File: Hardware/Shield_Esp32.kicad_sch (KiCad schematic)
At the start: 47 parts, among them J1 Conn_01x02_Male, J10 Conn_01x02_Male, J11 Conn_01x02_Male, J12 Conn_01x02_Male, J13 Conn_01x02_Male, J14 Conn_01x02_Male, J15 Conn_01x02_Male, J16 Conn_01x02_Male, J17 Conn_01x02_Male, J18 Conn_01x02_Male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

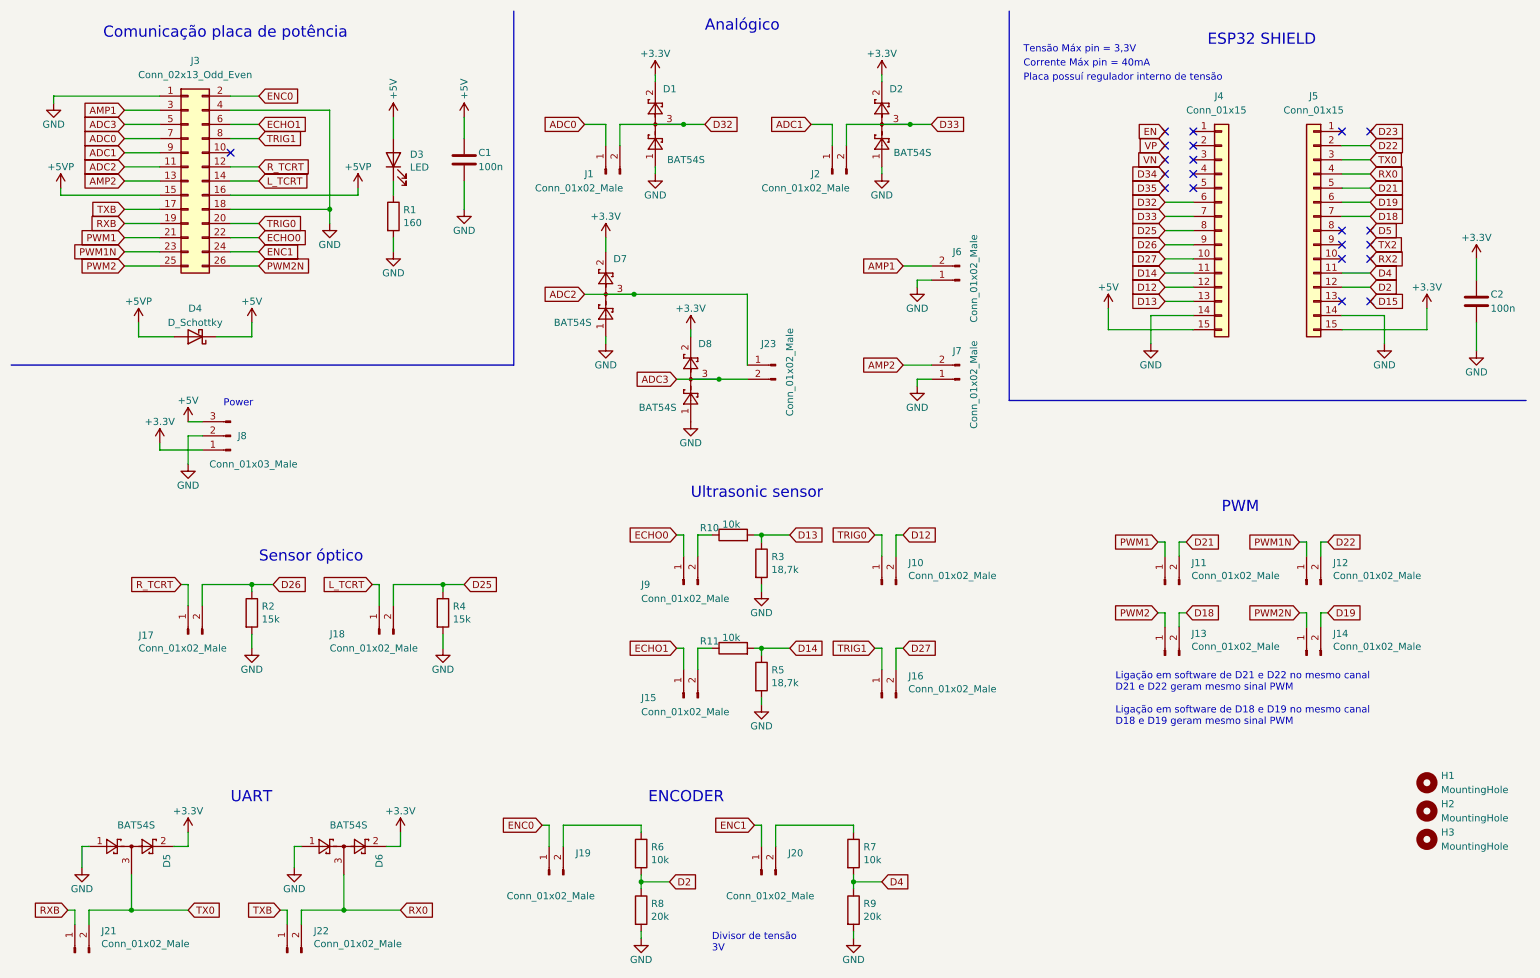
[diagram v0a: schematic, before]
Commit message: correção pino encoder
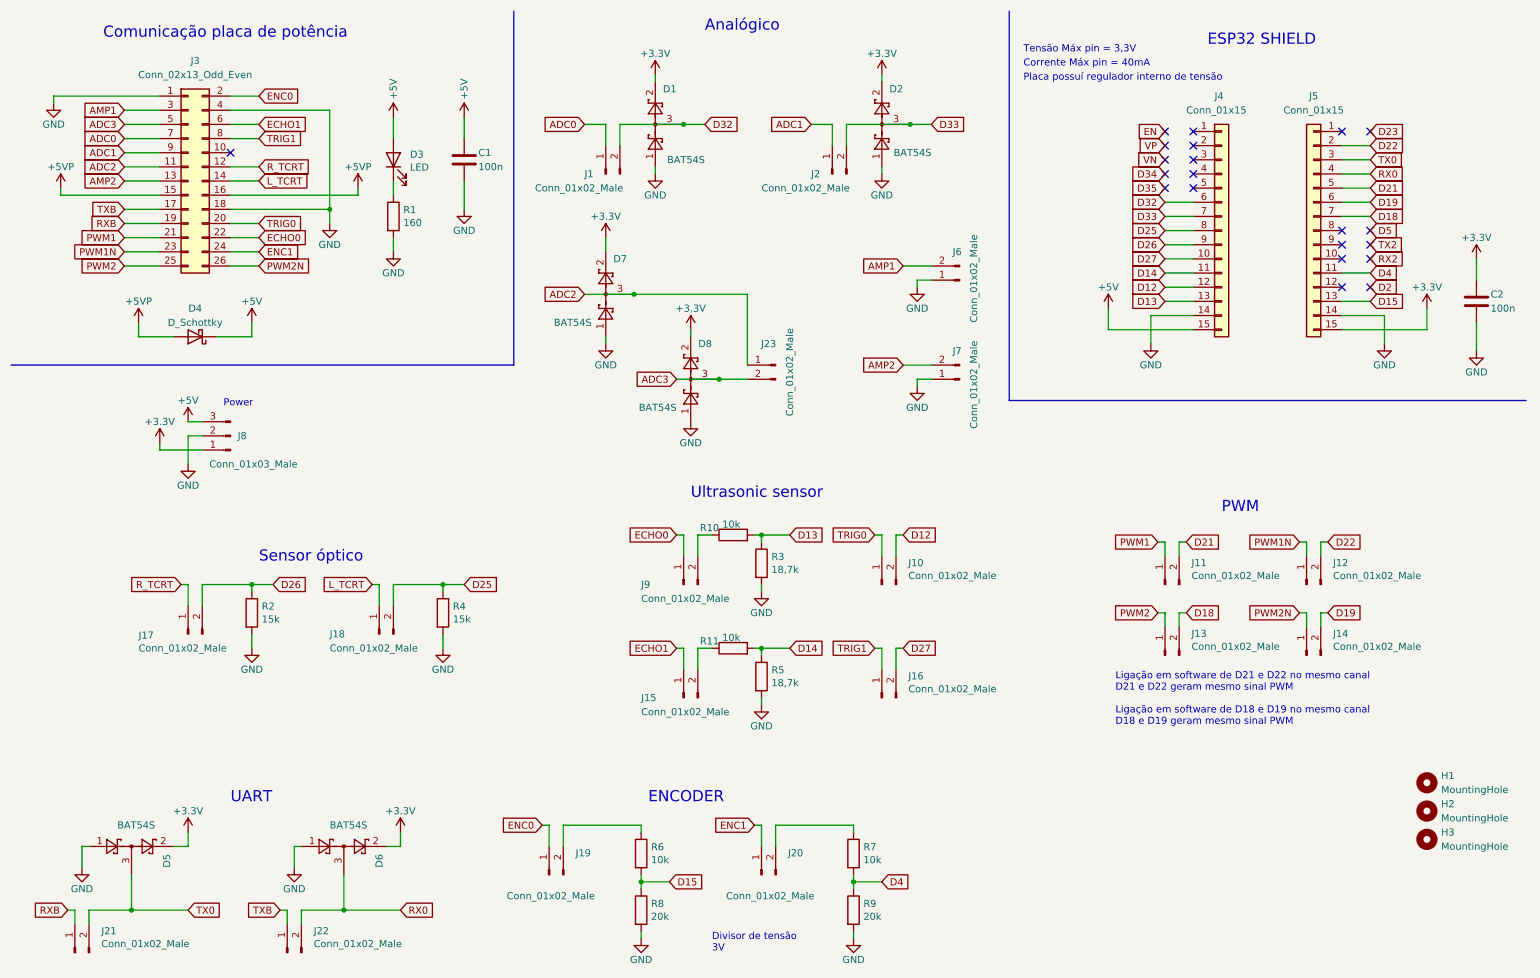
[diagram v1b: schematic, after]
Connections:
- net D15: now also J5.13 (Pin_13), R6.2, R8.1
- net D2: no longer J5.12 (Pin_12), R6.2, R8.1
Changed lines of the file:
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@@
   (no_connect (at 224.79 44.45))
   (no_connect (at 52.07 38.1))
+  (no_connect (at 256.54 62.23))
+  (no_connect (at 251.46 62.23))
   (no_connect (at 251.46 52.07))
   (no_connect (at 251.46 54.61))
   (no_connect (at 251.46 57.15))
-  (no_connect (at 251.46 64.77))
   (no_connect (at 256.54 52.07))
   (no_connect (at 256.54 34.29))
   (no_connect (at 251.46 34.29))
-  (no_connect (at 256.54 64.77))
   (no_connect (at 256.54 57.15))
   (no_connect (at 256.54 54.61))
@@
     (stroke (width 0) (type default) (color 0 0 0 0))
   )
-  (wire (pts (xy 251.46 62.23) (xy 256.54 62.23))
-    (stroke (width 0) (type default) (color 0 0 0 0))
-  )
   (wire (pts (xy 74.93 45.72) (xy 52.07 45.72))
     (stroke (width 0) (type default) (color 0 0 0 0))
@@
   )
   (wire (pts (xy 26.67 173.99) (xy 26.67 176.53))
+    (stroke (width 0) (type default) (color 0 0 0 0))
+  )
+  (wire (pts (xy 251.46 64.77) (xy 256.54 64.77))
     (stroke (width 0) (type default) (color 0 0 0 0))
   )
@@
     )
   )
-  (global_label "D2" (shape input) (at 130.81 168.91 0) (fields_autoplaced)
+  (global_label "D15" (shape input) (at 130.81 168.91 0) (fields_autoplaced)
     (effects (font (size 1.27 1.27)) (justify left))
-    (property "Intersheet References" "${INTERSHEET_REFS}" (id 0) (at 135.7026 168.8306 0)
+    (property "Intersheet References" "${INTERSHEET_REFS}" (id 0) (at 136.9121 168.8306 0)
       (effects (font (size 1.27 1.27)) (justify left) hide)
     )

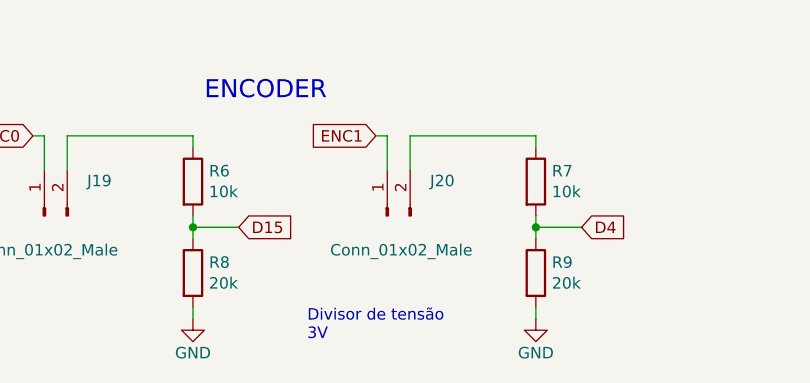
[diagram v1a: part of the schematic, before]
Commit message: mudança pino encoder
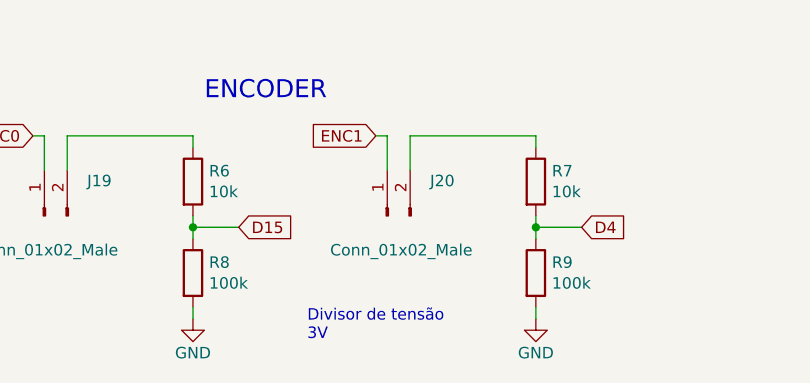
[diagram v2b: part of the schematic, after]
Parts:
- R8, R9: value 20k -> 100k
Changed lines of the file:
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@@
       (effects (font (size 1.27 1.27)) (justify left))
     )
-    (property "Value" "20k" (id 1) (at 127.508 175.133 0)
+    (property "Value" "100k" (id 1) (at 127.508 175.133 0)
       (effects (font (size 1.27 1.27)) (justify left))
     )
@@
       (effects (font (size 1.27 1.27)) (justify left))
     )
-    (property "Value" "20k" (id 1) (at 165.608 175.133 0)
+    (property "Value" "100k" (id 1) (at 165.608 175.133 0)
       (effects (font (size 1.27 1.27)) (justify left))
     )
@@
     )
     (path "/8cc10a9a-2477-4232-996c-c25bf899d45f"
-      (reference "R8") (unit 1) (value "20k") (footprint "Resistor_SMD:R_0805_2012Metric")
+      (reference "R8") (unit 1) (value "100k") (footprint "Resistor_SMD:R_0805_2012Metric")
     )
     (path "/9050431d-caa7-4f21-aaf0-07d9d33e1446"
-      (reference "R9") (unit 1) (value "20k") (footprint "Resistor_SMD:R_0805_2012Metric")
+      (reference "R9") (unit 1) (value "100k") (footprint "Resistor_SMD:R_0805_2012Metric")
     )
     (path "/6ba7466b-3e6d-4a1a-bec1-33e4e97e49b6"
